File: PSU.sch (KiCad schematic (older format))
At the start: 14 parts

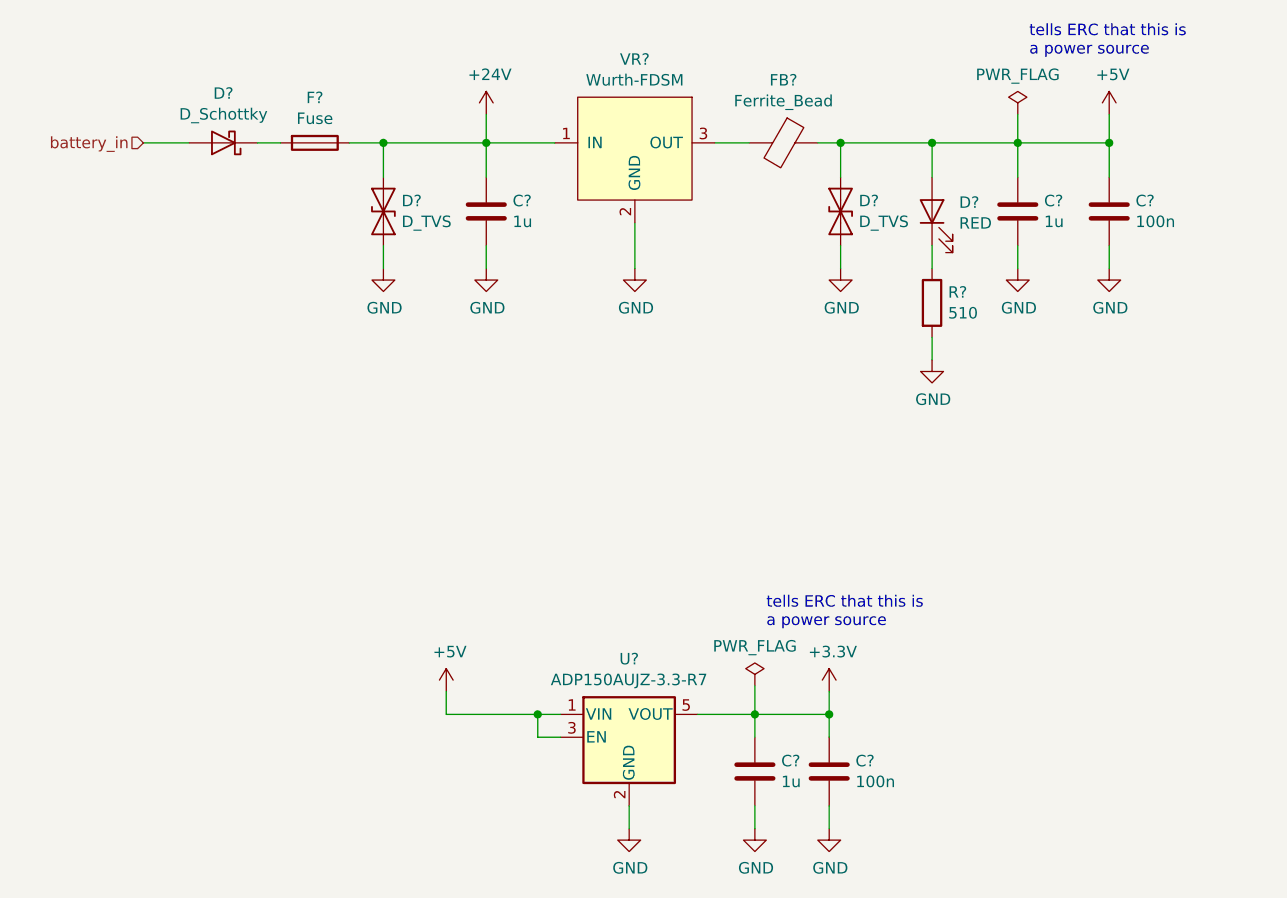
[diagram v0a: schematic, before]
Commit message: Fixed weird hierarchical sheets
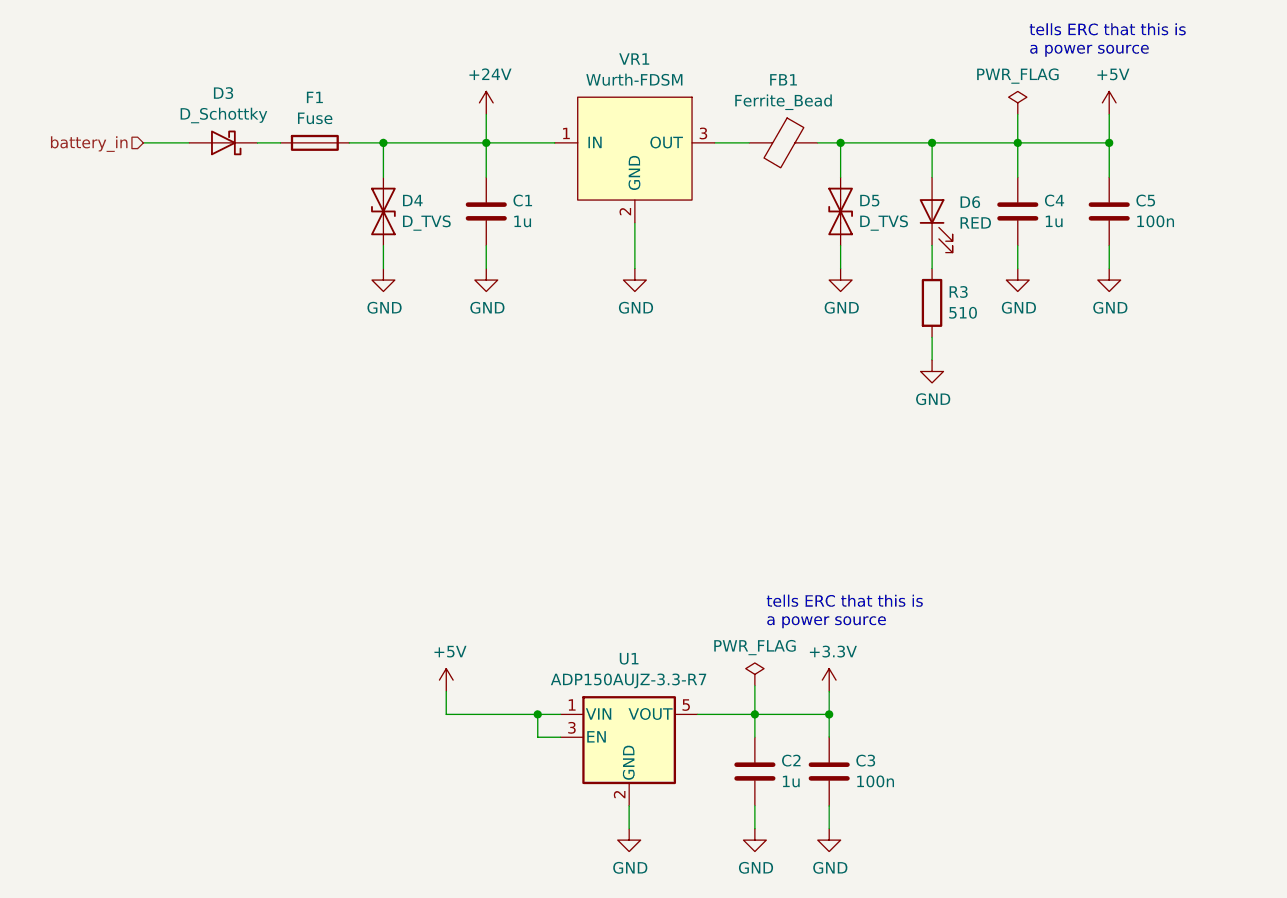
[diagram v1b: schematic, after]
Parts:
- gave numbers to parts that had none: 14
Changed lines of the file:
@@
 $Descr A4 11693 8268
 encoding utf-8
-Sheet 5 6
+Sheet 3 6
 Title ""
 Date ""
@@
 $EndDescr
 $Comp
-L KTHFS:Wurth-FDSM VR?
+L KTHFS:Wurth-FDSM VR1
 U 1 1 5DE8DC71
 P 5850 2075
-F 0 "VR?" H 5850 2440 50  0000 C CNN
+F 0 "VR1" H 5850 2440 50  0000 C CNN
 F 1 "Wurth-FDSM" H 5850 2349 50  0000 C CNN
 F 2 "KTHFS:Wurth-FDSM" H 5550 2225 50  0001 C CNN
@@
 battery_in
 $Comp
-L Device:Fuse F?
+L Device:Fuse F1
 U 1 1 5DE8E0CA
 P 4450 2075
-F 0 "F?" V 4253 2075 50  0000 C CNN
+F 0 "F1" V 4253 2075 50  0000 C CNN
 F 1 "Fuse" V 4344 2075 50  0000 C CNN
 F 2 "" V 4380 2075 50  0001 C CNN
@@
 $EndComp
 $Comp
-L Device:D_Schottky D?
+L Device:D_Schottky D3
 U 1 1 5DE8E836
 P 4050 2075
-F 0 "D?" H 4050 1859 50  0000 C CNN
+F 0 "D3" H 4050 1859 50  0000 C CNN
 F 1 "D_Schottky" H 4050 1950 50  0000 C CNN
 F 2 "" H 4050 2075 50  0001 C CNN
@@
 $EndComp
 $Comp
-L Device:D_TVS D?
+L Device:D_TVS D4
 U 1 1 5DE8F267
 P 4750 2375
-F 0 "D?" V 4704 2454 50  0000 L CNN
+F 0 "D4" V 4704 2454 50  0000 L CNN
 F 1 "D_TVS" V 4795 2454 50  0000 L CNN
 F 2 "" H 4750 2375 50  0001 C CNN
@@
 	4200 2075 4300 2075
 $Comp
-L Device:C C?
+L Device:C C1
 U 1 1 5DE9088B
 P 5200 2375
-F 0 "C?" H 5315 2421 50  0000 L CNN
+F 0 "C1" H 5315 2421 50  0000 L CNN
 F 1 "1u" H 5315 2330 50  0000 L CNN
 F 2 "" H 5238 2225 50  0001 C CNN
@@
 Connection ~ 5200 2075
 $Comp
-L power:GND #PWR?
+L power:GND #PWR0106
 U 1 1 5DE931F9
 P 5850 2625
-F 0 "#PWR?" H 5850 2375 50  0001 C CNN
+F 0 "#PWR0106" H 5850 2375 50  0001 C CNN
 F 1 "GND" H 5855 2452 50  0000 C CNN
 F 2 "" H 5850 2625 50  0001 C CNN
@@
 	5850 2625 5850 2425
 $Comp
-L power:GND #PWR?
+L power:GND #PWR0107
 U 1 1 5DE935C5
 P 5200 2625
-F 0 "#PWR?" H 5200 2375 50  0001 C CNN
+F 0 "#PWR0107" H 5200 2375 50  0001 C CNN
 F 1 "GND" H 5205 2452 50  0000 C CNN
 F 2 "" H 5200 2625 50  0001 C CNN
@@
 	5200 2625 5200 2525
 $Comp
-L power:GND #PWR?
+L power:GND #PWR0108
 U 1 1 5DE93ED3
 P 4750 2625
-F 0 "#PWR?" H 4750 2375 50  0001 C CNN
+F 0 "#PWR0108" H 4750 2375 50  0001 C CNN
 F 1 "GND" H 4755 2452 50  0000 C CNN
 F 2 "" H 4750 2625 50  0001 C CNN
@@
 	6750 2225 6750 2075
 $Comp
-L Device:C C?
+L Device:C C4
 U 1 1 5DE96837
 P 7525 2375
-F 0 "C?" H 7640 2421 50  0000 L CNN
+F 0 "C4" H 7640 2421 50  0000 L CNN
 F 1 "1u" H 7640 2330 50  0000 L CNN
 F 2 "" H 7563 2225 50  0001 C CNN
@@
 	7525 2225 7525 2075
 $Comp
-L power:+24V #PWR?
+L power:+24V #PWR0109
 U 1 1 5DE9891F
 P 5200 1950
-F 0 "#PWR?" H 5200 1800 50  0001 C CNN
+F 0 "#PWR0109" H 5200 1800 50  0001 C CNN
 F 1 "+24V" H 5215 2123 50  0000 C CNN
 F 2 "" H 5200 1950 50  0001 C CNN
@@
 	5200 1950 5200 2075
 $Comp
-L power:+5V #PWR?
+L power:+5V #PWR0110
 U 1 1 5DE99120
 P 7925 1950
-F 0 "#PWR?" H 7925 1800 50  0001 C CNN
+F 0 "#PWR0110" H 7925 1800 50  0001 C CNN
 F 1 "+5V" H 7940 2123 50  0000 C CNN
 F 2 "" H 7925 1950 50  0001 C CNN
@@
 $EndComp
 $Comp
-L Device:C C?
+L Device:C C5
 U 1 1 5DE99784
 P 7925 2375
-F 0 "C?" H 8040 2421 50  0000 L CNN
+F 0 "C5" H 8040 2421 50  0000 L CNN
 F 1 "100n" H 8040 2330 50  0000 L CNN
 F 2 "" H 7963 2225 50  0001 C CNN
@@
 Connection ~ 7525 2075
 $Comp
-L power:GND #PWR?
+L power:GND #PWR0111
 U 1 1 5DE9A7DE
 P 7525 2625
-F 0 "#PWR?" H 7525 2375 50  0001 C CNN
+F 0 "#PWR0111" H 7525 2375 50  0001 C CNN
 F 1 "GND" H 7530 2452 50  0000 C CNN
 F 2 "" H 7525 2625 50  0001 C CNN
@@
 	7525 2625 7525 2525
 $Comp
-L power:GND #PWR?
+L power:GND #PWR0112
 U 1 1 5DE9AC7B
 P 7925 2625
-F 0 "#PWR?" H 7925 2375 50  0001 C CNN
+F 0 "#PWR0112" H 7925 2375 50  0001 C CNN
 F 1 "GND" H 7930 2452 50  0000 C CNN
 F 2 "" H 7925 2625 50  0001 C CNN
@@
 	7925 2625 7925 2525
 $Comp
-L power:PWR_FLAG #FLG?
+L power:PWR_FLAG #FLG0101
 U 1 1 5DE9B17C
 P 7525 1950
-F 0 "#FLG?" H 7525 2025 50  0001 C CNN
+F 0 "#FLG0101" H 7525 2025 50  0001 C CNN
 F 1 "PWR_FLAG" H 7525 2123 50  0000 C CNN
 F 2 "" H 7525 1950 50  0001 C CNN
@@
 Connection ~ 7925 2075
 $Comp
-L Device:Ferrite_Bead FB?
+L Device:Ferrite_Bead FB1
 U 1 1 5DEA6FED
 P 6500 2075
-F 0 "FB?" V 6226 2075 50  0000 C CNN
+F 0 "FB1" V 6226 2075 50  0000 C CNN
 F 1 "Ferrite_Bead" V 6317 2075 50  0000 C CNN
 F 2 "" V 6430 2075 50  0001 C CNN
@@
 	6750 2075 7150 2075
 $Comp
-L Device:LED D?
+L Device:LED D6
 U 1 1 5DEA538C
 P 7150 2375
-F 0 "D?" V 7189 2257 50  0000 R CNN
+F 0 "D6" V 7189 2257 50  0000 R CNN
 F 1 "RED" V 7098 2257 50  0000 R CNN
 F 2 "" H 7150 2375 50  0001 C CNN
@@
 $EndComp
 $Comp
-L Device:R R?
+L Device:R R3
 U 1 1 5DEA6286
 P 7150 2775
-F 0 "R?" H 7220 2821 50  0000 L CNN
+F 0 "R3" H 7220 2821 50  0000 L CNN
 F 1 "510" H 7220 2730 50  0000 L CNN
 F 2 "" V 7080 2775 50  0001 C CNN
@@
 	7150 2525 7150 2625
 $Comp
-L power:GND #PWR?
+L power:GND #PWR0113
 U 1 1 5DEA756F
 P 7150 3025
-F 0 "#PWR?" H 7150 2775 50  0001 C CNN
+F 0 "#PWR0113" H 7150 2775 50  0001 C CNN
 F 1 "GND" H 7155 2852 50  0000 C CNN
 F 2 "" H 7150 3025 50  0001 C CNN
@@
 	6750 2625 6750 2525
 $Comp
-L power:GND #PWR?
+L power:GND #PWR0114
 U 1 1 5DE9A361
 P 6750 2625
-F 0 "#PWR?" H 6750 2375 50  0001 C CNN
+F 0 "#PWR0114" H 6750 2375 50  0001 C CNN
 F 1 "GND" H 6755 2452 50  0000 C CNN
 F 2 "" H 6750 2625 50  0001 C CNN
@@
 $EndComp
 $Comp
-L Device:D_TVS D?
+L Device:D_TVS D5
 U 1 1 5DE95FEA
 P 6750 2375
-F 0 "D?" V 6704 2454 50  0000 L CNN
+F 0 "D5" V 6704 2454 50  0000 L CNN
 F 1 "D_TVS" V 6795 2454 50  0000 L CNN
 F 2 "" H 6750 2375 50  0001 C CNN
@@
 $EndComp
 $Comp
-L KTHFS:ADP150AUJZ-3.3-R7 U?
+L KTHFS:ADP150AUJZ-3.3-R7 U1
 U 1 1 5DEAE8EA
 P 5825 4675
-F 0 "U?" H 5825 5017 50  0000 C CNN
+F 0 "U1" H 5825 5017 50  0000 C CNN
 F 1 "ADP150AUJZ-3.3-R7" H 5825 4926 50  0000 C CNN
 F 2 "Package_TO_SOT_SMD:SOT-23-5" H 5825 5000 50  0001 C CIN
@@
 	5025 4475 5025 4575
 $Comp
-L power:+5V #PWR?
+L power:+5V #PWR0115
 U 1 1 5DEAEF2D
 P 5025 4475
-F 0 "#PWR?" H 5025 4325 50  0001 C CNN
+F 0 "#PWR0115" H 5025 4325 50  0001 C CNN
 F 1 "+5V" H 5040 4648 50  0000 C CNN
 F 2 "" H 5025 4475 50  0001 C CNN
@@
 $EndComp
 $Comp
-L Device:C C?
+L Device:C C3
 U 1 1 5DEAF625
 P 6700 4825
-F 0 "C?" H 6815 4871 50  0000 L CNN
+F 0 "C3" H 6815 4871 50  0000 L CNN
 F 1 "100n" H 6815 4780 50  0000 L CNN
 F 2 "" H 6738 4675 50  0001 C CNN
@@
 Connection ~ 6700 4575
 $Comp
-L power:GND #PWR?
+L power:GND #PWR0116
 U 1 1 5DEAFB22
 P 5825 5075
-F 0 "#PWR?" H 5825 4825 50  0001 C CNN
+F 0 "#PWR0116" H 5825 4825 50  0001 C CNN
 F 1 "GND" H 5830 4902 50  0000 C CNN
 F 2 "" H 5825 5075 50  0001 C CNN
@@
 	6700 4475 6700 4575
 $Comp
-L power:GND #PWR?
+L power:GND #PWR0117
 U 1 1 5DEB1F96
 P 6700 5075
-F 0 "#PWR?" H 6700 4825 50  0001 C CNN
+F 0 "#PWR0117" H 6700 4825 50  0001 C CNN
 F 1 "GND" H 6705 4902 50  0000 C CNN
 F 2 "" H 6700 5075 50  0001 C CNN
@@
 AR Path="/5DE839B2/5DEB3867" Ref="#FLG?"  Part="1"
 AR Path="/5DE839FC/5DEB3867" Ref="#FLG?"  Part="1"
-F 0 "#FLG?" H 6375 4525 50  0001 C CNN
+AR Path="/60145B96/5DEB3867" Ref="#FLG0102"  Part="1"
+F 0 "#FLG0102" H 6375 4525 50  0001 C CNN
 F 1 "PWR_FLAG" H 6375 4623 50  0000 C CNN
 F 2 "" H 6375 4450 50  0001 C CNN
@@
 	6375 4575 6700 4575
 $Comp
-L Device:C C?
+L Device:C C2
 U 1 1 5DEB39A3
 P 6375 4825
-F 0 "C?" H 6490 4871 50  0000 L CNN
+F 0 "C2" H 6490 4871 50  0000 L CNN
 F 1 "1u" H 6490 4780 50  0000 L CNN
 F 2 "" H 6413 4675 50  0001 C CNN
@@
 	6375 5075 6375 4975
 $Comp
-L power:GND #PWR?
+L power:GND #PWR0118
 U 1 1 5DEB42A4
 P 6375 5075
-F 0 "#PWR?" H 6375 4825 50  0001 C CNN
+F 0 "#PWR0118" H 6375 4825 50  0001 C CNN
 F 1 "GND" H 6380 4902 50  0000 C CNN
 F 2 "" H 6375 5075 50  0001 C CNN
@@
 	6375 4675 6375 4575
 $Comp
-L power:+3.3V #PWR?
+L power:+3.3V #PWR0119
 U 1 1 5DEAF1B9
 P 6700 4475
-F 0 "#PWR?" H 6700 4325 50  0001 C CNN
+F 0 "#PWR0119" H 6700 4325 50  0001 C CNN
 F 1 "+3.3V" H 6715 4648 50  0000 C CNN
 F 2 "" H 6700 4475 50  0001 C CNN

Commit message: Changes to PA layout
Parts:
- C1, C2, C3, C4, C5: footprint (none) -> Capacitor_SMD:C_0603_1608Metric
- R3: footprint (none) -> Resistor_SMD:R_0603_1608Metric
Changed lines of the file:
@@
 F 0 "C1" H 5315 2421 50  0000 L CNN
 F 1 "1u" H 5315 2330 50  0000 L CNN
-F 2 "" H 5238 2225 50  0001 C CNN
+F 2 "Capacitor_SMD:C_0603_1608Metric" H 5238 2225 50  0001 C CNN
 F 3 "~" H 5200 2375 50  0001 C CNN
 	1    5200 2375
@@
 F 0 "C4" H 7640 2421 50  0000 L CNN
 F 1 "1u" H 7640 2330 50  0000 L CNN
-F 2 "" H 7563 2225 50  0001 C CNN
+F 2 "Capacitor_SMD:C_0603_1608Metric" H 7563 2225 50  0001 C CNN
 F 3 "~" H 7525 2375 50  0001 C CNN
 	1    7525 2375
@@
 F 0 "C5" H 8040 2421 50  0000 L CNN
 F 1 "100n" H 8040 2330 50  0000 L CNN
-F 2 "" H 7963 2225 50  0001 C CNN
+F 2 "Capacitor_SMD:C_0603_1608Metric" H 7963 2225 50  0001 C CNN
 F 3 "~" H 7925 2375 50  0001 C CNN
 	1    7925 2375
@@
 F 0 "R3" H 7220 2821 50  0000 L CNN
 F 1 "510" H 7220 2730 50  0000 L CNN
-F 2 "" V 7080 2775 50  0001 C CNN
+F 2 "Resistor_SMD:R_0603_1608Metric" V 7080 2775 50  0001 C CNN
 F 3 "~" H 7150 2775 50  0001 C CNN
 	1    7150 2775
@@
 F 0 "C3" H 6815 4871 50  0000 L CNN
 F 1 "100n" H 6815 4780 50  0000 L CNN
-F 2 "" H 6738 4675 50  0001 C CNN
+F 2 "Capacitor_SMD:C_0603_1608Metric" H 6738 4675 50  0001 C CNN
 F 3 "~" H 6700 4825 50  0001 C CNN
 	1    6700 4825
@@
 F 0 "C2" H 6490 4871 50  0000 L CNN
 F 1 "1u" H 6490 4780 50  0000 L CNN
-F 2 "" H 6413 4675 50  0001 C CNN
+F 2 "Capacitor_SMD:C_0603_1608Metric" H 6413 4675 50  0001 C CNN
 F 3 "~" H 6375 4825 50  0001 C CNN
 	1    6375 4825

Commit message: Lots of work on routing and pcb layout
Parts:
- C1, C2: footprint Capacitor_SMD:C_0603_1608Metric -> Capacitor_SMD:C_0805_2012Metric
- D3, D4, D5, D6: footprint (none) -> Diode_SMD:D_SOD-323
- F1: footprint (none) -> Fuse:Fuse_0805_2012Metric
- FB1: footprint (none) -> Capacitor_SMD:C_0805_2012Metric
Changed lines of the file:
@@
 F 0 "F1" V 4253 2075 50  0000 C CNN
 F 1 "Fuse" V 4344 2075 50  0000 C CNN
-F 2 "" V 4380 2075 50  0001 C CNN
+F 2 "Fuse:Fuse_0805_2012Metric" V 4380 2075 50  0001 C CNN
 F 3 "~" H 4450 2075 50  0001 C CNN
 	1    4450 2075
@@
 F 0 "D3" H 4050 1859 50  0000 C CNN
 F 1 "D_Schottky" H 4050 1950 50  0000 C CNN
-F 2 "" H 4050 2075 50  0001 C CNN
+F 2 "Diode_SMD:D_SOD-323" H 4050 2075 50  0001 C CNN
 F 3 "~" H 4050 2075 50  0001 C CNN
 	1    4050 2075
@@
 F 0 "D4" V 4704 2454 50  0000 L CNN
 F 1 "D_TVS" V 4795 2454 50  0000 L CNN
-F 2 "" H 4750 2375 50  0001 C CNN
+F 2 "Diode_SMD:D_SOD-323" H 4750 2375 50  0001 C CNN
 F 3 "~" H 4750 2375 50  0001 C CNN
 	1    4750 2375
@@
 F 0 "C1" H 5315 2421 50  0000 L CNN
 F 1 "1u" H 5315 2330 50  0000 L CNN
-F 2 "Capacitor_SMD:C_0603_1608Metric" H 5238 2225 50  0001 C CNN
+F 2 "Capacitor_SMD:C_0805_2012Metric" H 5238 2225 50  0001 C CNN
 F 3 "~" H 5200 2375 50  0001 C CNN
 	1    5200 2375
@@
 	7525 2225 7525 2075
 $Comp
-L power:+24V #PWR0109
-U 1 1 5DE9891F
-P 5200 1950
-F 0 "#PWR0109" H 5200 1800 50  0001 C CNN
-F 1 "+24V" H 5215 2123 50  0000 C CNN
-F 2 "" H 5200 1950 50  0001 C CNN
-F 3 "" H 5200 1950 50  0001 C CNN
-	1    5200 1950
-	1    0    0    -1
-$EndComp
-Wire Wire Line
-	5200 1950 5200 2075
-$Comp
 L power:+5V #PWR0110
 U 1 1 5DE99120
@@
 F 0 "FB1" V 6226 2075 50  0000 C CNN
 F 1 "Ferrite_Bead" V 6317 2075 50  0000 C CNN
-F 2 "" V 6430 2075 50  0001 C CNN
+F 2 "Capacitor_SMD:C_0805_2012Metric" V 6430 2075 50  0001 C CNN
 F 3 "~" H 6500 2075 50  0001 C CNN
 	1    6500 2075
@@
 F 0 "D6" V 7189 2257 50  0000 R CNN
 F 1 "RED" V 7098 2257 50  0000 R CNN
-F 2 "" H 7150 2375 50  0001 C CNN
+F 2 "Diode_SMD:D_SOD-323" H 7150 2375 50  0001 C CNN
 F 3 "~" H 7150 2375 50  0001 C CNN
 	1    7150 2375
@@
 F 0 "D5" V 6704 2454 50  0000 L CNN
 F 1 "D_TVS" V 6795 2454 50  0000 L CNN
-F 2 "" H 6750 2375 50  0001 C CNN
+F 2 "Diode_SMD:D_SOD-323" H 6750 2375 50  0001 C CNN
 F 3 "~" H 6750 2375 50  0001 C CNN
 	1    6750 2375
@@
 F 0 "C2" H 6490 4871 50  0000 L CNN
 F 1 "1u" H 6490 4780 50  0000 L CNN
-F 2 "Capacitor_SMD:C_0603_1608Metric" H 6413 4675 50  0001 C CNN
+F 2 "Capacitor_SMD:C_0805_2012Metric" H 6413 4675 50  0001 C CNN
 F 3 "~" H 6375 4825 50  0001 C CNN
 	1    6375 4825
@@
 	1    0    0    -1
 $EndComp
+Wire Wire Line
+	5200 1950 5200 2075
+$Comp
+L power:+24V #PWR0109
+U 1 1 5DE9891F
+P 5200 1950
+F 0 "#PWR0109" H 5200 1800 50  0001 C CNN
+F 1 "+24V" H 5215 2123 50  0000 C CNN
+F 2 "" H 5200 1950 50  0001 C CNN
+F 3 "" H 5200 1950 50  0001 C CNN
+	1    5200 1950
+	1    0    0    -1
+$EndComp

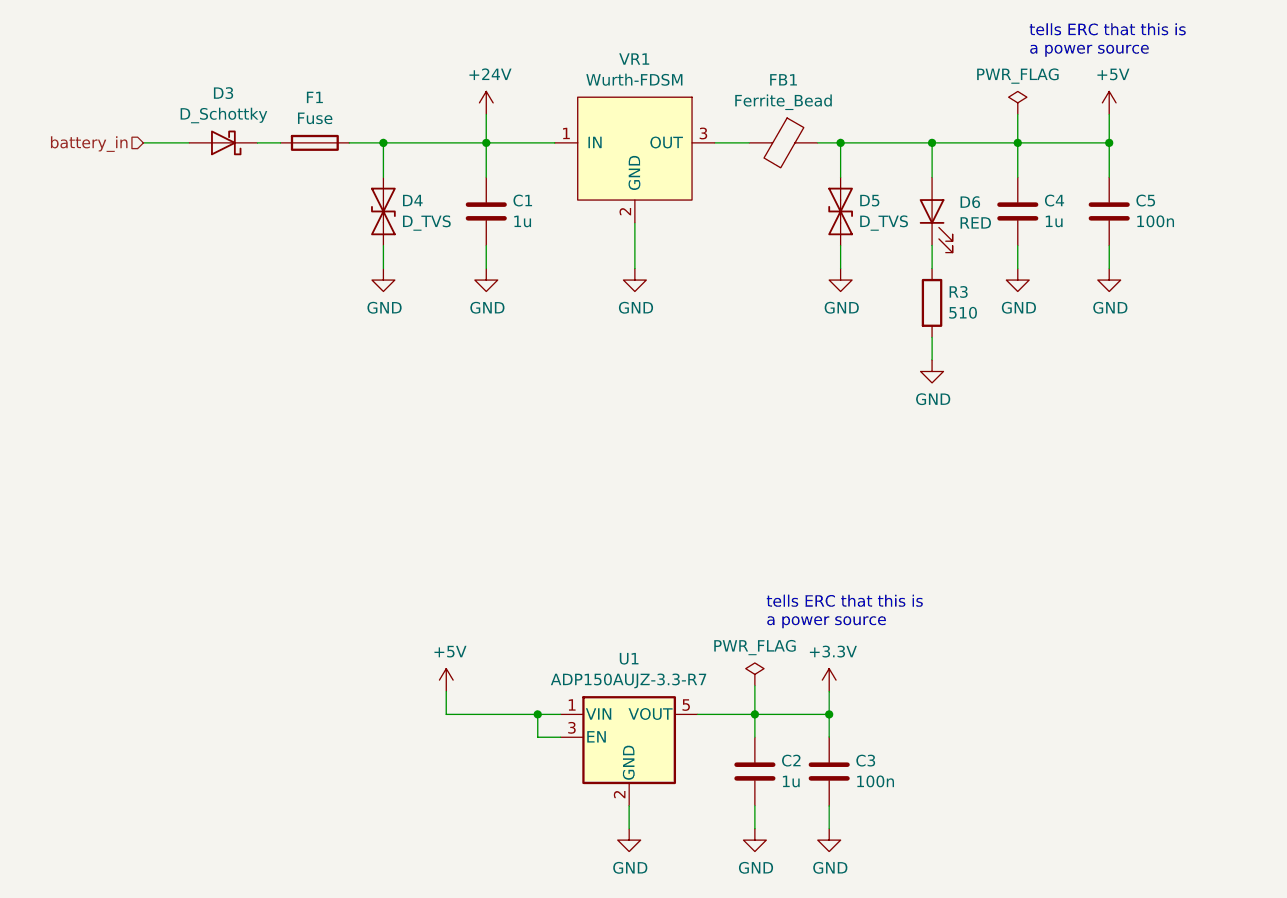
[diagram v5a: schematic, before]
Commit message: Fixed (most) pwr flag issues
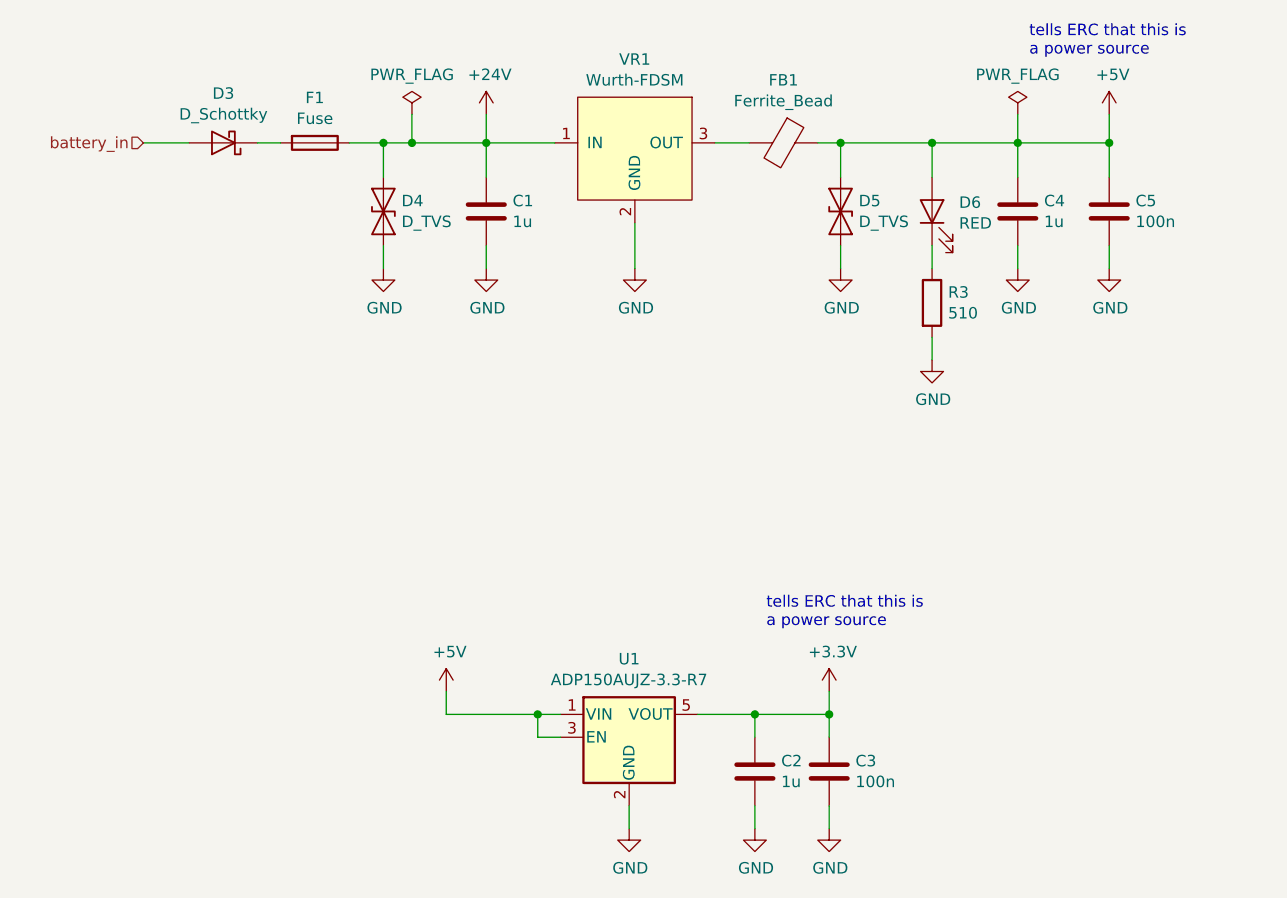
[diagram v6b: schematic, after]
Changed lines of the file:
@@
 	5200 2225 5200 2075
 Wire Wire Line
-	5200 2075 4750 2075
+	5200 2075 4875 2075
 Connection ~ 4750 2075
 Wire Wire Line
@@
 	1    0    0    -1
 $EndComp
-Wire Wire Line
-	6375 4450 6375 4575
-$Comp
-L power:PWR_FLAG #FLG?
-U 1 1 5DEB3867
-P 6375 4450
-AR Path="/5DE839B2/5DEB3867" Ref="#FLG?"  Part="1"
-AR Path="/5DE839FC/5DEB3867" Ref="#FLG?"  Part="1"
-AR Path="/60145B96/5DEB3867" Ref="#FLG0102"  Part="1"
-F 0 "#FLG0102" H 6375 4525 50  0001 C CNN
-F 1 "PWR_FLAG" H 6375 4623 50  0000 C CNN
-F 2 "" H 6375 4450 50  0001 C CNN
-F 3 "~" H 6375 4450 50  0001 C CNN
-	1    6375 4450
-	1    0    0    -1
-$EndComp
+$Comp
+L power:PWR_FLAG #FLG0103
+U 1 1 602DA6A7
+P 4875 1950
+F 0 "#FLG0103" H 4875 2025 50  0001 C CNN
+F 1 "PWR_FLAG" H 4875 2123 50  0000 C CNN
+F 2 "" H 4875 1950 50  0001 C CNN
+F 3 "~" H 4875 1950 50  0001 C CNN
+	1    4875 1950
+	1    0    0    -1
+$EndComp
+Wire Wire Line
+	4875 1950 4875 2075
+Connection ~ 4875 2075
+Wire Wire Line
+	4875 2075 4750 2075
 $EndSCHEMATC
